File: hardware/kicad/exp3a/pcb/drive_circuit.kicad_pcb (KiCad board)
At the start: 2 copper layers, 134 x 60 mm, 14 parts, among them J1 PWM ind, J2 forsyning, M1 Motor_DC, Q1 IRF540N, U1 ILD74, U2 IR2110

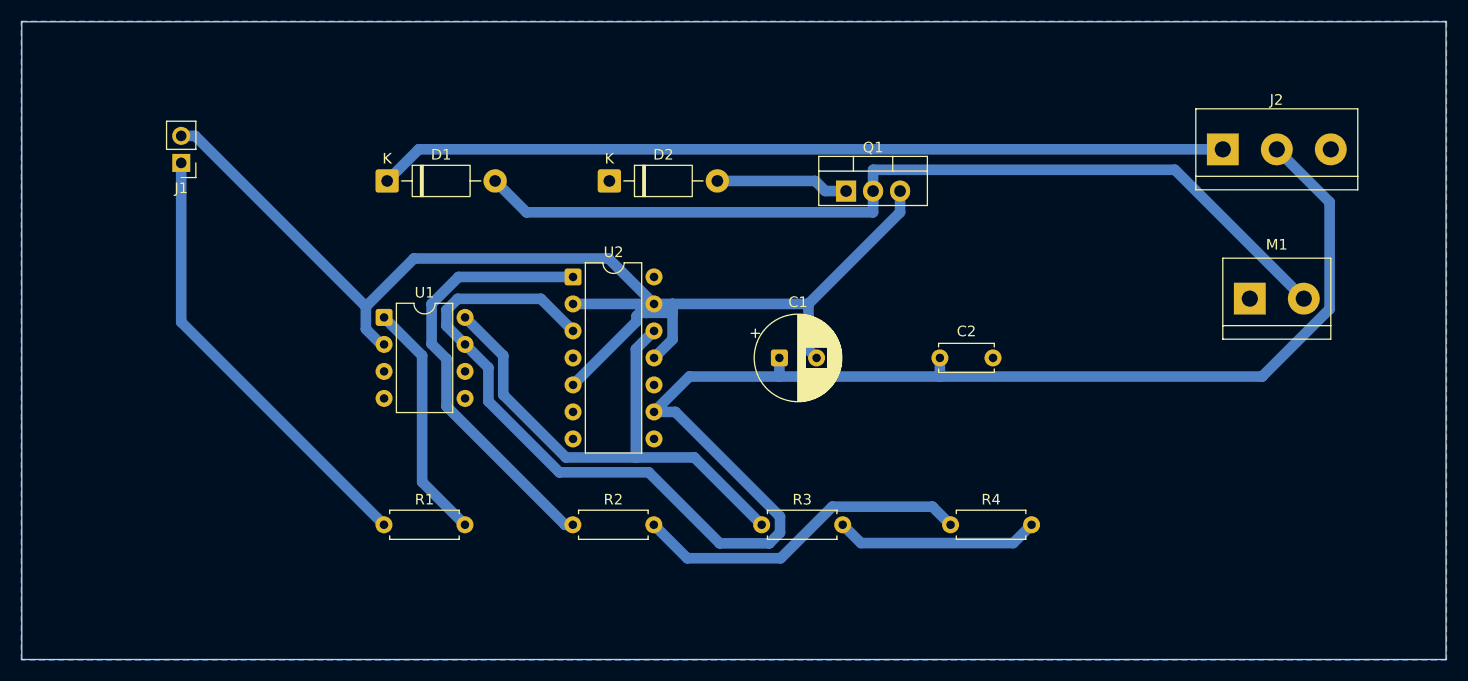
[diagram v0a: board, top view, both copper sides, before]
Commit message: Apply fiber-laser design rules from the DTU-PCB-prototyping guide
All seven boards rebuilt to meet the XTool fiber laser workflow
(SimsesLab/DTU-PCB-prototyping): 1.0 mm tracks, 0.8 mm clearance, solid
no-net fill zone on B.Cu (pad connection: none) so the laser only
engraves the isolation channels, DIP footprints switched to the
_LongPads variants from the guide's shop table.

TO packages cannot meet 0.8 mm pad-to-pad at stock sizes, so
energy_system.pretty now has TO-220-3_Vertical_LaserPads (pads narrowed
to 1.7 mm -> 0.84 mm gap; make_laserpads.py regenerates). The MPPT pass
transistor moves BD139 -> TIP41A (shop part): TO-126's 2.28 mm pitch can
never satisfy the rule, and TO-220 handles the ~7 W better anyway.

Two more bugs caught in this pass:
- Device:Q_NMOS uses letter pin numbers (G/D/S) while TO-220 pads are
  1/2/3 - buck/boost MOSFET pads silently got NO net in the earlier
  boards (no-net pads don't count as unconnected). pcb_build.py now maps
  G/D/S->1/2/3 and fails hard if a component ends up netless.
- DRC now 0 violations on all seven boards; remaining airwires are the
  documented jumpers.
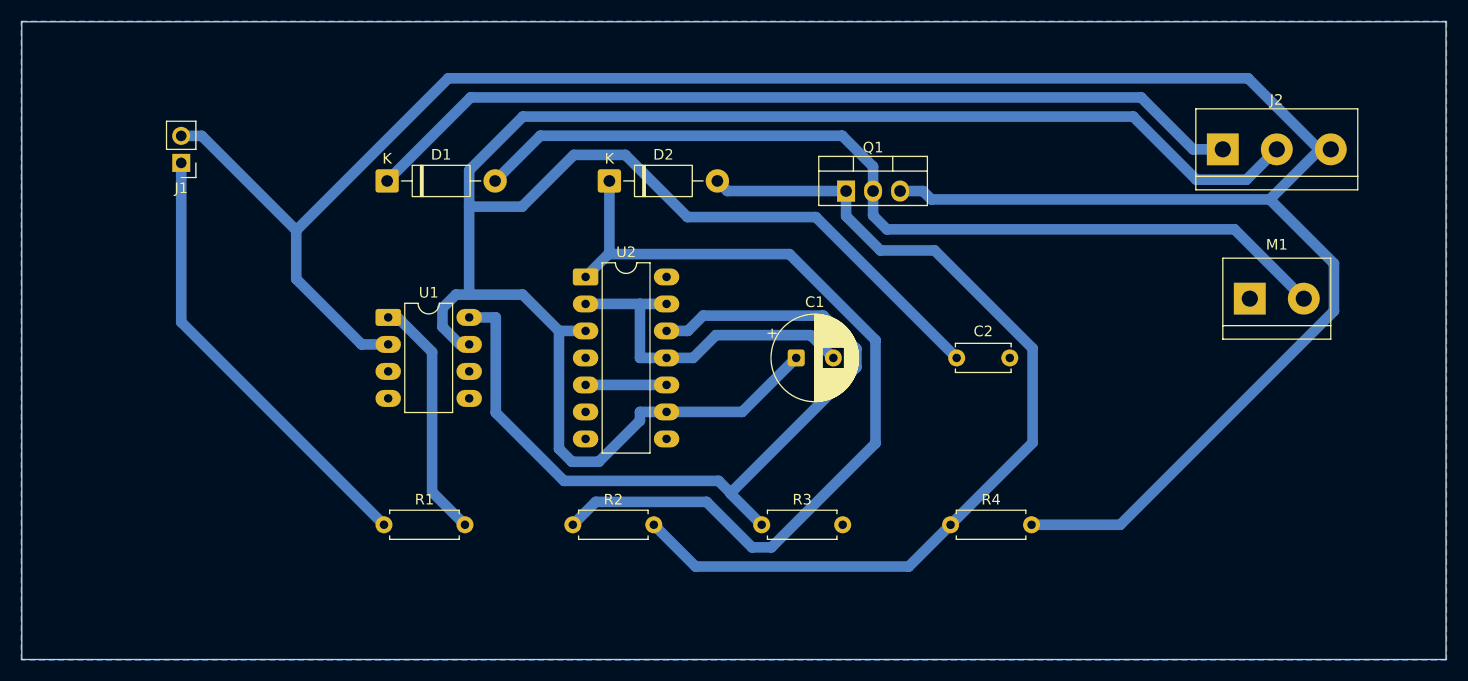
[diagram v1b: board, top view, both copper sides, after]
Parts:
- Q1: footprint TO-220-3_Vertical -> TO-220-3_Vertical_LaserPads
- U1: footprint DIP-8_W7.62mm -> DIP-8_W7.62mm_LongPads
- U2: footprint DIP-14_W7.62mm -> DIP-14_W7.62mm_LongPads
- moved C1 1.58 mm to (92.9, 51.6)
- moved C2 1.58 mm to (108.0, 51.6)
- moved U2 1.18 mm to (73.0, 44.0)
- moved U1 0.39 mm to (54.5, 47.8)
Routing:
- net GND: track 138.4 -> 268.2 mm
- net +15V: track 162.8 -> 208.0 mm
- net Net-(D2-A): track 44.4 -> 88.5 mm
- net Net-(D2-K): track 41.1 -> 83.3 mm
- net Net-(U2-LIN): track 50.8 -> 79.1 mm
- net +20V: track 79.9 -> 83.9 mm
- net Net-(D1-A): track 86.3 -> 86.9 mm
- added copper zone on B.Cu, net (none)
- removed copper zone on B.Cu, net GND

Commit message: Engrave component references into the copper on all boards
The fiber laser has no silkscreen step, so the refdes (R1, U1, ...) are
placed as mirrored copper text on B.Cu next to each component - they
engrave in the same run as the traces and read correctly from the
solder side. Placement is collision-checked against tracks/pads/other
text (copper text over a track would short or sever it); tracks are
sampled into small boxes so diagonal runs don't false-positive. 86 of
96 labels fit; the handful dropped in dense spots are listed in
production/README.md and still appear on the F_Fab plots.

Also exports <board>_silk_top.dxf (F.Silkscreen + outline) per board as
an optional top-side engraving pass - run it on the component side
BEFORE the copper run, and do NOT mirror that one.

DRC still 0 violations on all seven; jumper lists updated.
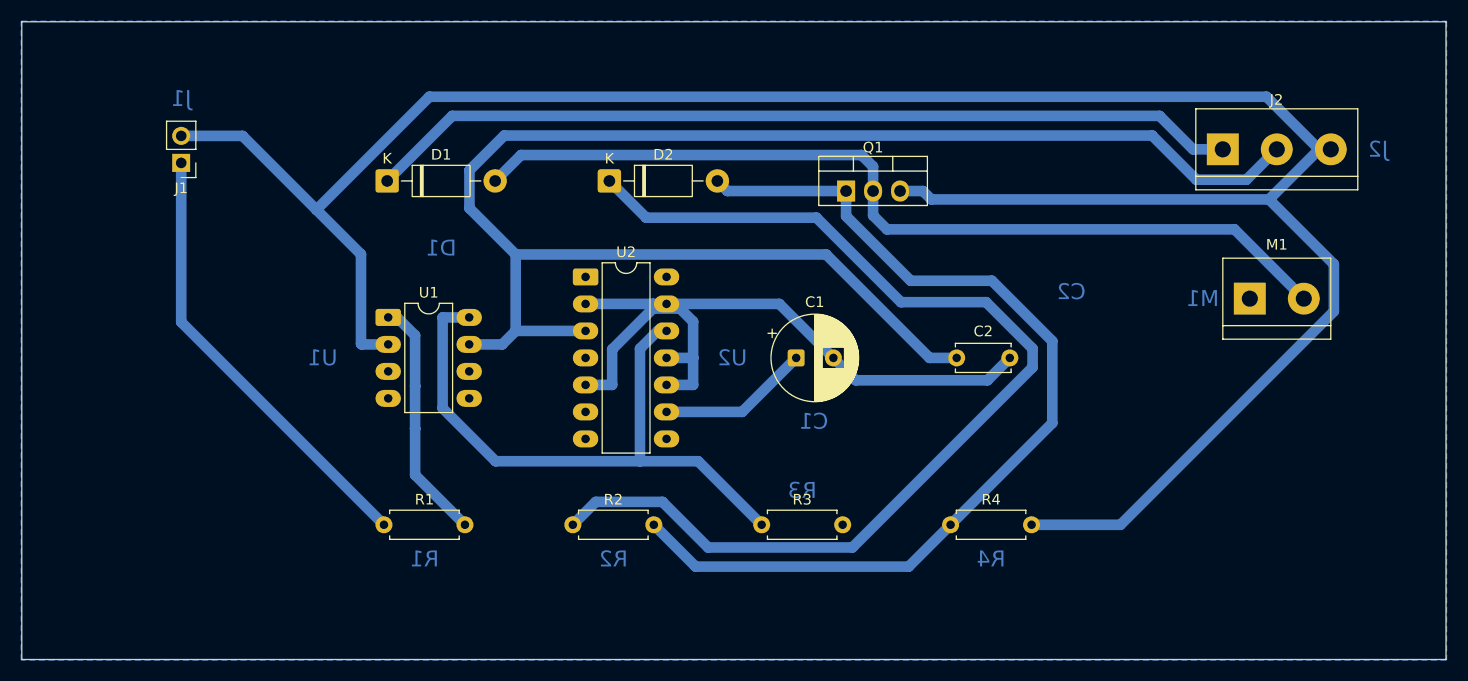
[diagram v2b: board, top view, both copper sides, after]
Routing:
- net +15V: track 208.0 -> 168.4 mm
- net GND: track 268.2 -> 296.7 mm
- net Net-(U2-LIN): track 79.1 -> 59.4 mm
- net Net-(D2-K): track 83.3 -> 101.1 mm
- net Net-(D2-A): track 88.5 -> 91.6 mm
- net Net-(D1-A): track 86.9 -> 85.4 mm
- net +20V: track 83.9 -> 82.5 mm
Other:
- board text added: "C1"
- board text added: "C2"
- board text added: "D1"
- board text added: "J1"
- board text added: "J2"
- board text added: "M1"
- board text added: "R1"
- board text added: "R2"
- board text added: "R3"
- board text added: "R4"
- board text added: "U1"
- board text added: "U2"
